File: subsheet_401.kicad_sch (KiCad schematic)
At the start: 16 parts, among them U401 STE_GSTSHIFTER_PHY

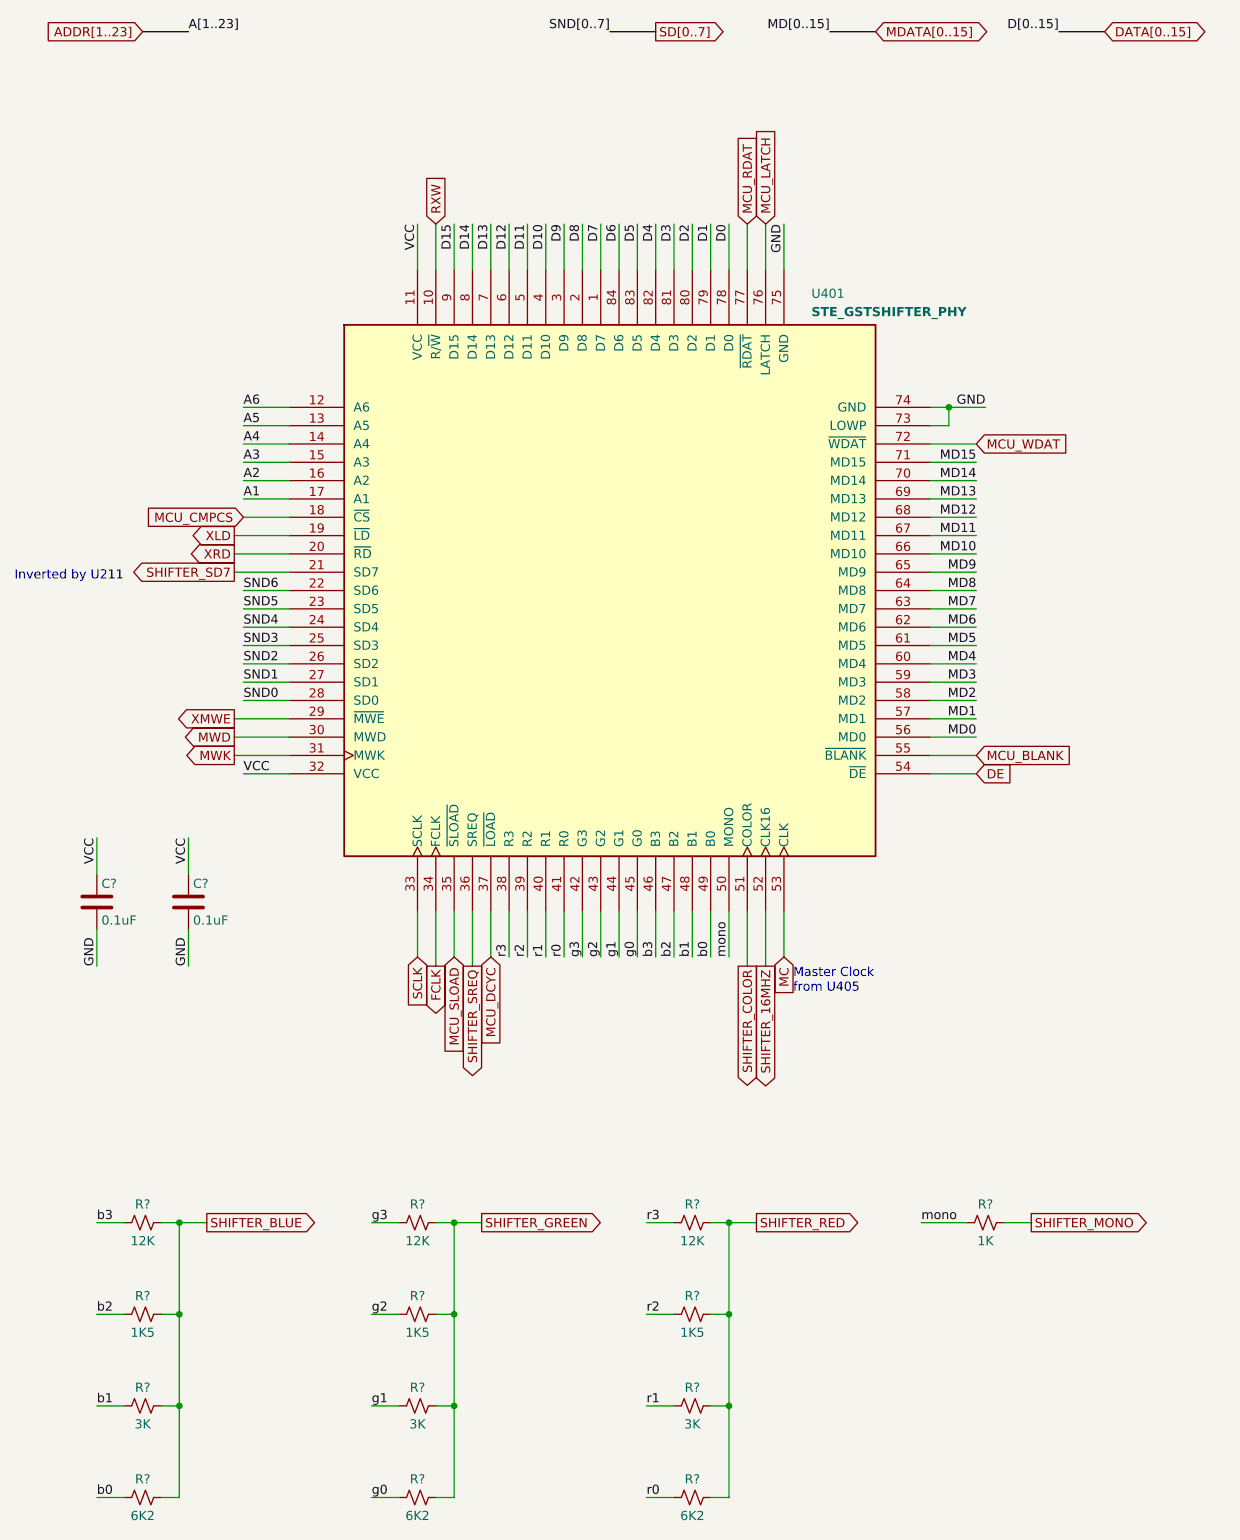
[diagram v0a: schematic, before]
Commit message: Resolves #3 : [schematic] annotate video port with signal name
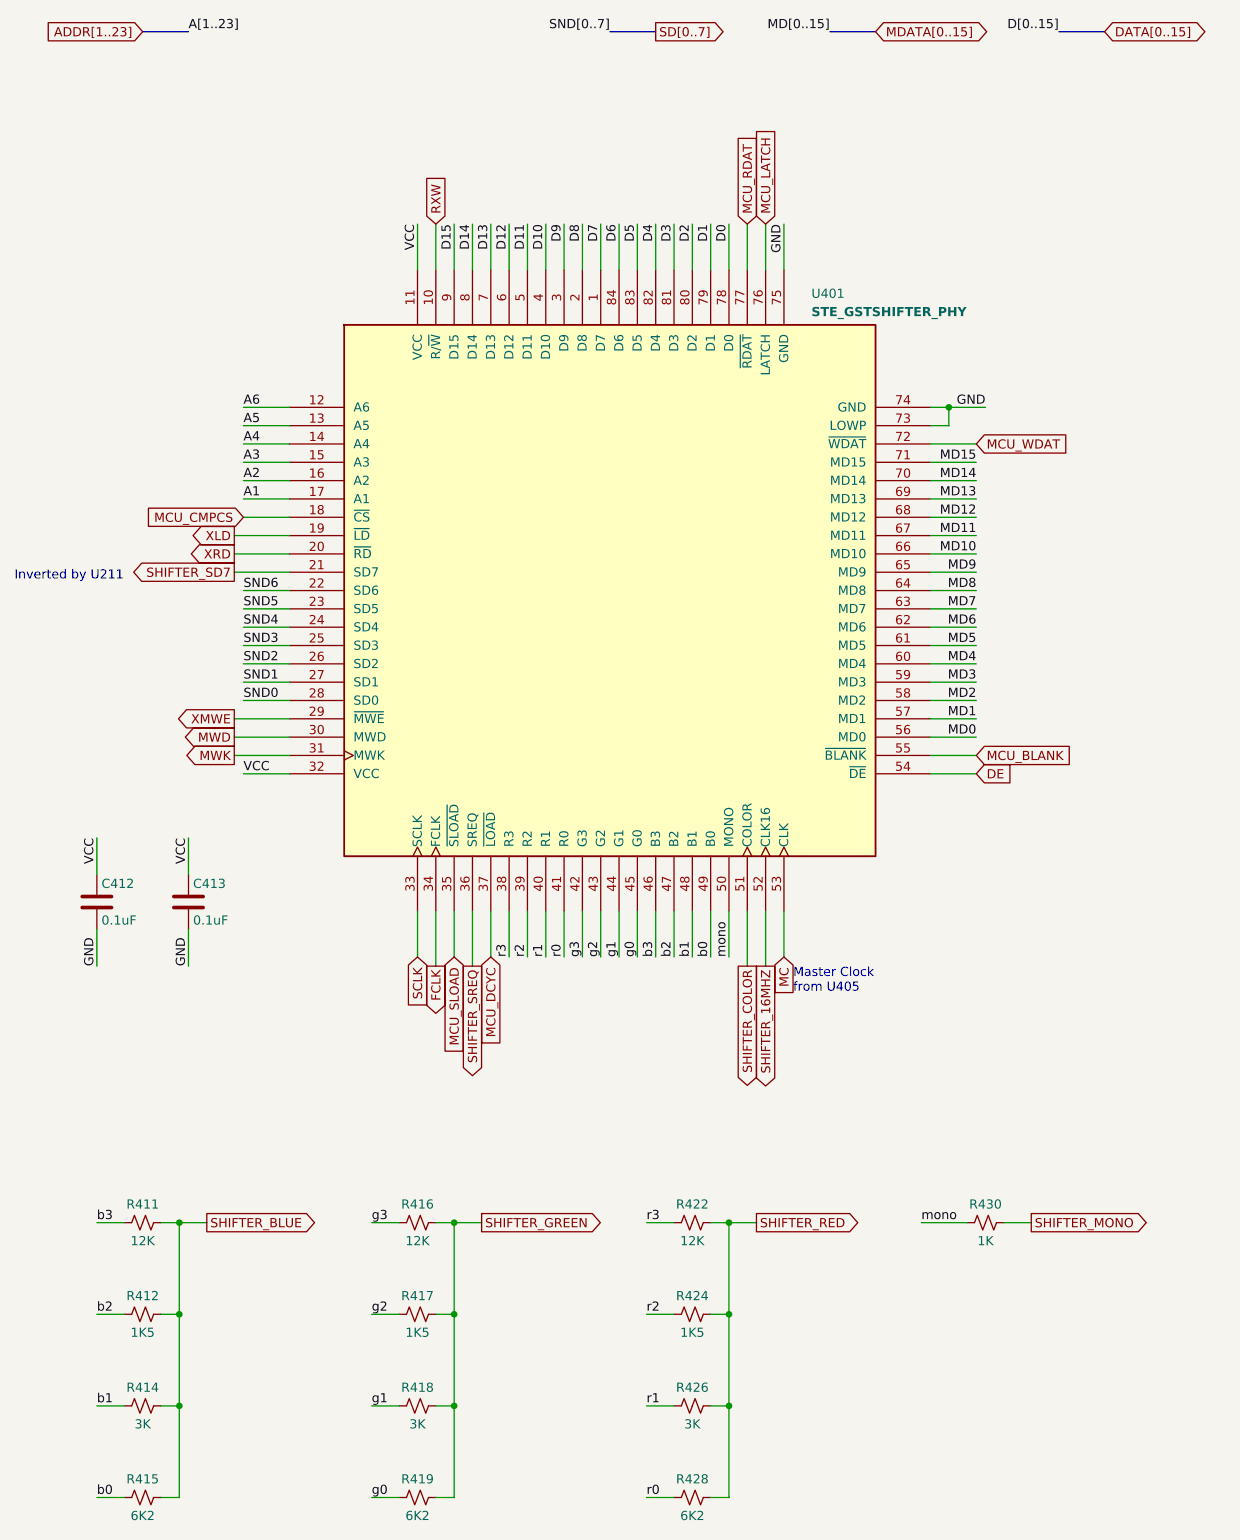
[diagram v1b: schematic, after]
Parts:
- gave numbers to parts that had none: 15
